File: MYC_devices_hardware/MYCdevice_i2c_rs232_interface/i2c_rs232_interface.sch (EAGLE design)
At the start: 60 parts, among them IC1 MEGA32-P, IC2 MAX232, IC3 7805TV, Q1 20MHz, T1 BC817, T2 BC817, T3 BC817, T4 BC807, T5 BC817-40LT1SMD, T6 BC817-40LT1SMD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

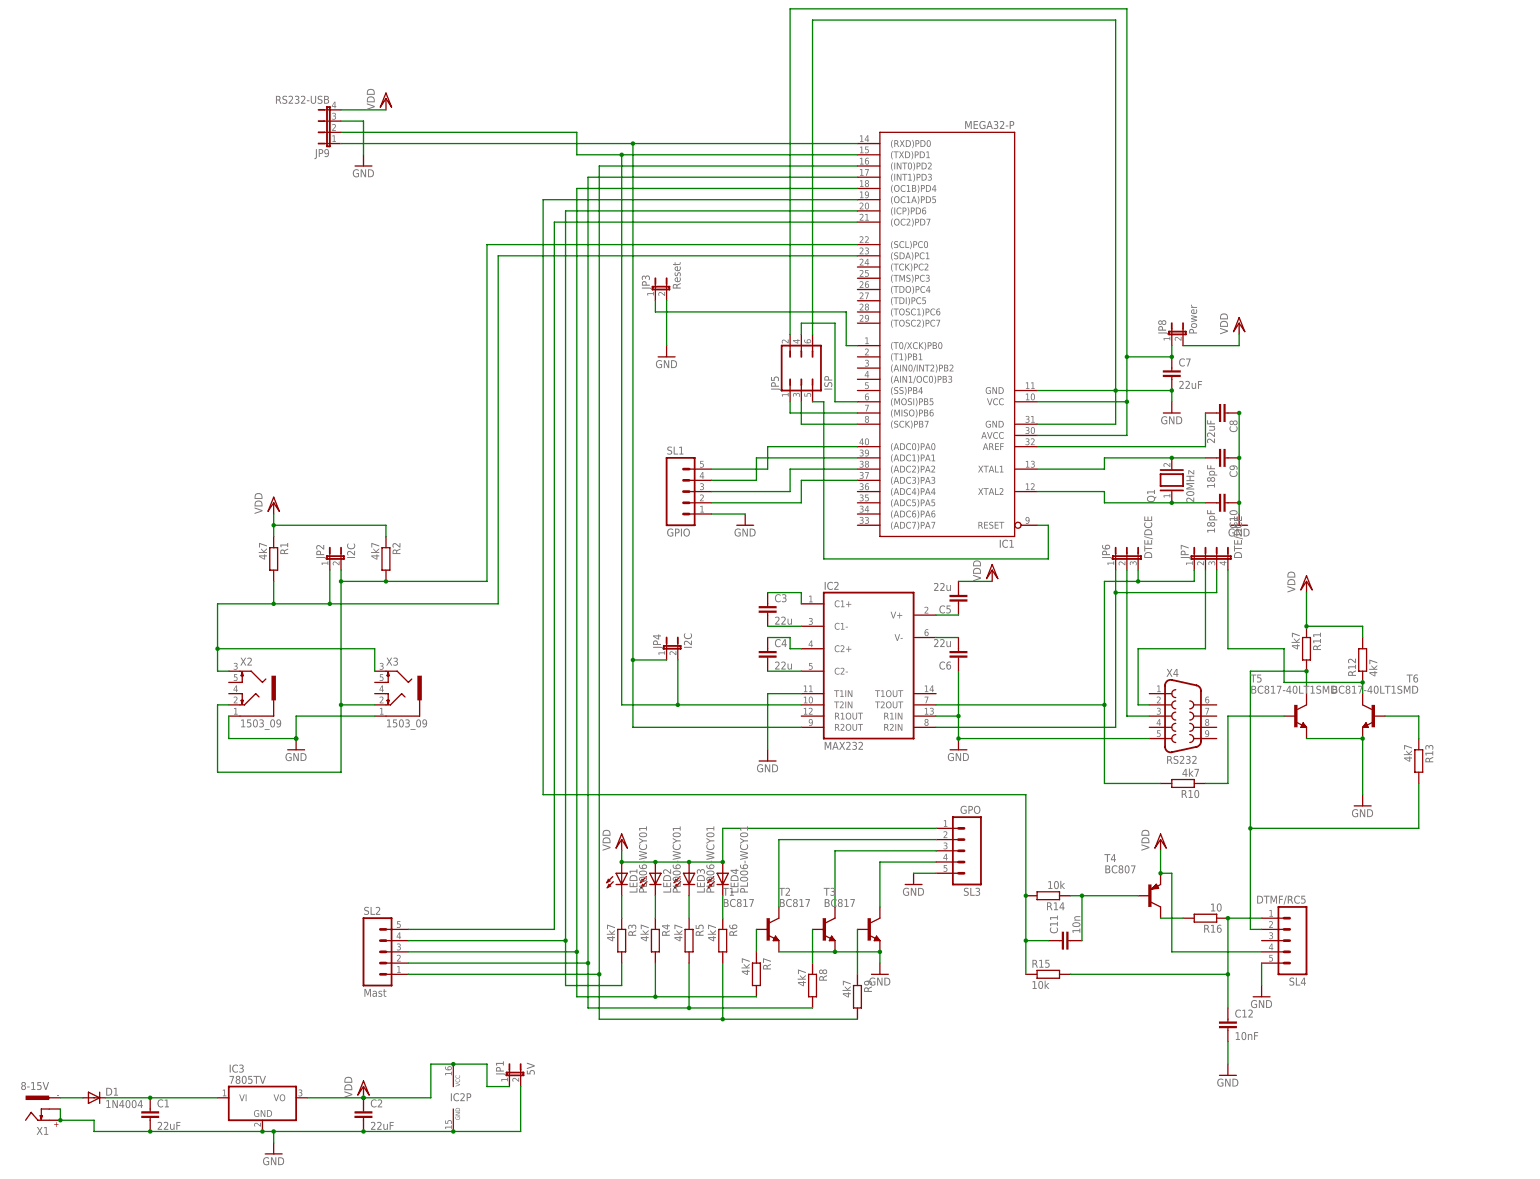
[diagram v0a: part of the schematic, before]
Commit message: HW changed and 254 /255 command croorected
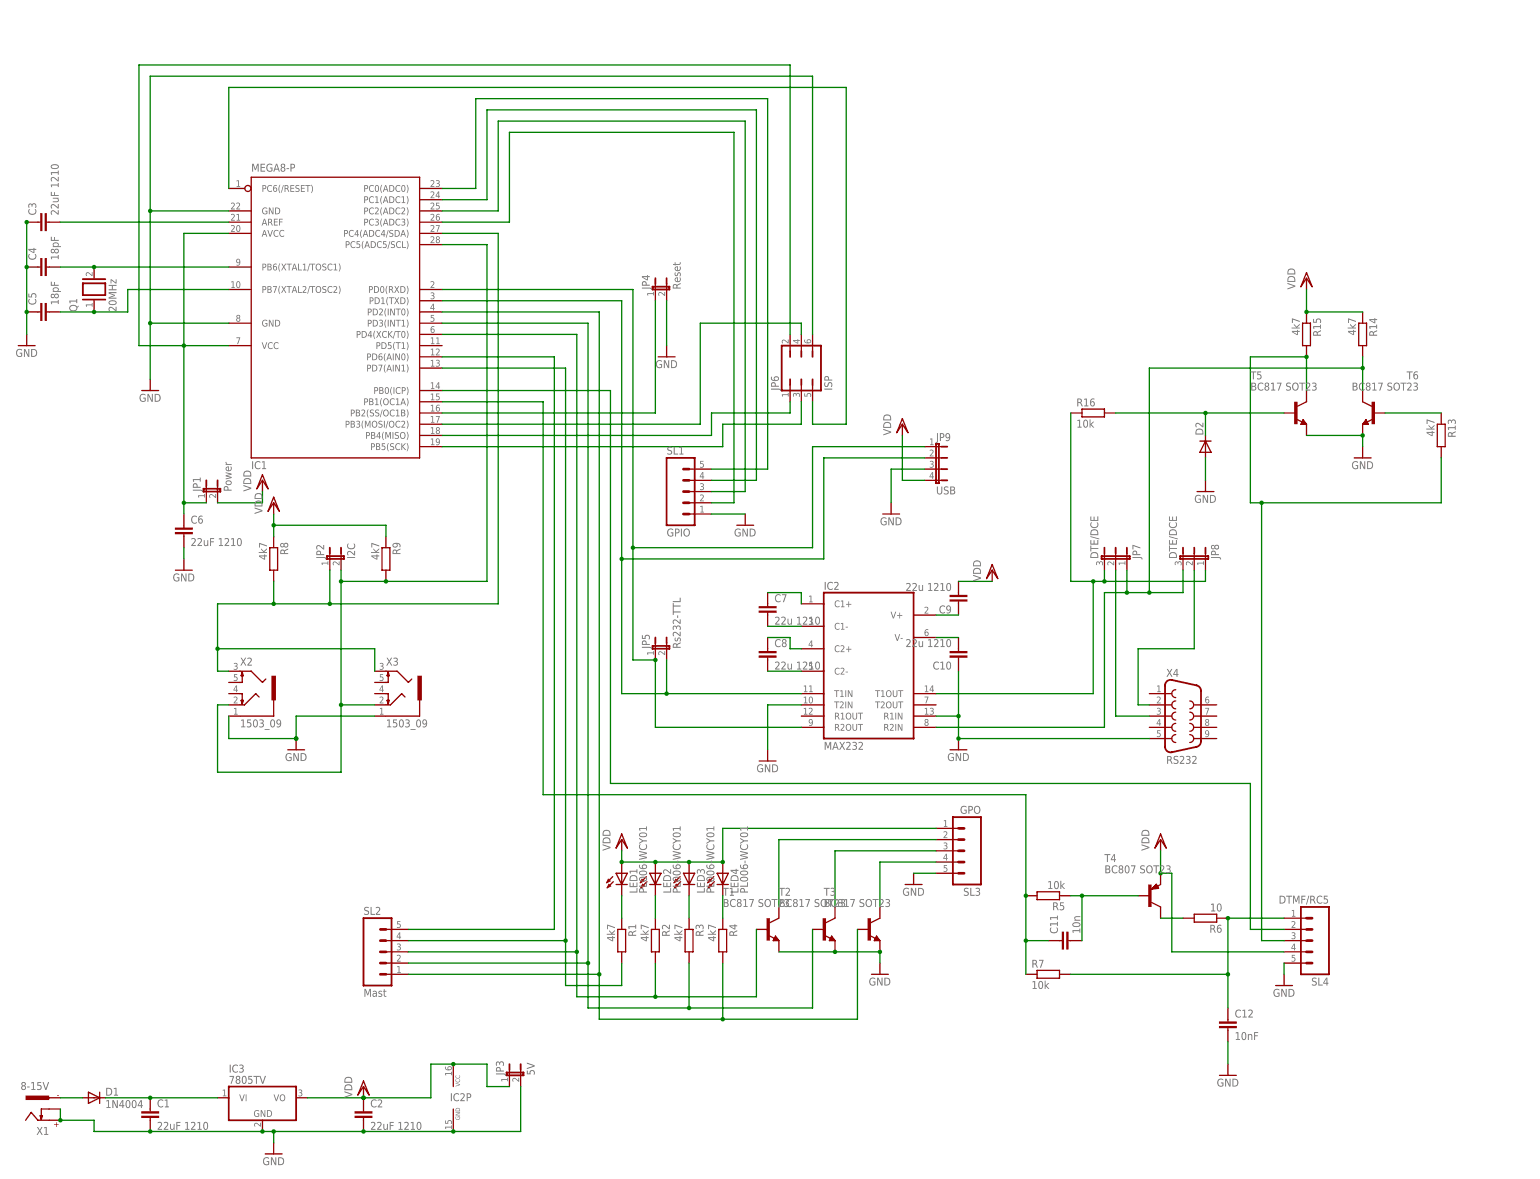
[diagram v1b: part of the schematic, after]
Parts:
- removed R10, R11, R12: 4k7, resistor:R-EU_0207/5V
- added D2: (no value), diode:DIODE-SOD106-R
- C1, C2: value 22uF -> 22uF 1210
- C10, C9: value 18pF -> 22u 1210; device resistor:C-EU025-025X050 -> rcl:C-EUC1206
- C3, C6: value 22u -> 22uF 1210
- C4, C5: value 22u -> 18pF; device rcl:C-EUC1206 -> resistor:C-EU025-025X050
- C7, C8: value 22uF -> 22u 1210
- IC1: value MEGA32-P -> MEGA8-P; device atmel:MEGA32-P -> atmel:MEGA8-P
- JP1: value 5V -> Power
- JP3: value Reset -> 5V
- JP4: value I2C -> Reset
- JP5: value ISP -> Rs232-TTL; device jumper:JP3Q -> jumper:JP1E
- JP6: value DTE/DCE -> ISP; device jumper:JP2E -> jumper:JP3Q
- JP7: device jumper:JP4E -> jumper:JP2E
- JP8: value Power -> DTE/DCE; device jumper:JP1E -> jumper:JP2E
- JP9: value RS232-USB -> USB
- R1, R13, R2, R3, R4: device resistor:R-EU_0207/5V -> resistor:R-EU_R1206
- R14, R15: value 10k -> 4k7; device resistor:R-EU_0207/5V -> resistor:R-EU_R1206
- R16: value 10 -> 10k; device resistor:R-EU_0207/5V -> resistor:R-EU_R1206
- R5, R7: value 4k7 -> 10k
- R6: value 4k7 -> 10
- T1, T2, T3: value BC817 -> BC817 SOT23
- T4: value BC807 -> BC807 SOT23
- T5, T6: value BC817-40LT1SMD -> BC817 SOT23; device transistor-npn:BC817-40LT1SMD -> transistor:BC817-NPN-SOT23-BEC
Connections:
- removed net N$11: IC2G$1.R2IN, JP6.1, JP7.3
- removed net N$21: JP7.4, R12.1, T6.C
- removed net N$24: R7.1, T1.B
- removed net N$27 (its old number): IC1.(RXD)PD0, IC2G$1.R2OUT, JP4.1, JP9.1
- removed net N$36: R11.2, R13.2, SL4.2, T5.C
- removed net N$40: R9.1, T3.B
- removed net N$42 (its old number): C8.2, IC1.AREF
- removed net N$55: C10.2, IC1.XTAL2, Q1.1
- removed net N$58: C7.1, IC1.AVCC, IC1.VCC, JP5.2, JP8.1
- new net N$10: IC2G$1.T1OUT, JP7.3, JP8.1, R16.1
- new net N$37: C5.2, IC1.PB7(XTAL2/TOSC2), Q1.1
- new net N$38: D2.C, R16.2, T5.B
- new net N$44: C6.1, IC1.AVCC, IC1.VCC@1, JP1.1, JP6.2
- new net N$53: R13.2, R15.2, SL4.3, T5.C
- new net N$7: IC1.PB0(ICP), SL4.2
- net C13: now also C7.1; no longer C3.1
- net GND: now also C3.1, C4.1, C5.1, C6.2, D2.A, IC2G$1.T2IN, JP4.2, JP6.6; no longer C6.1, C7.2, C8.1, C9.1, IC2G$1.T1IN, JP1.2, JP5.6
- net N$1: now also IC1.PD7(AIN1), R1.2; no longer IC1.(ICP)PD6, R3.2
- net N$12: now also IC1.PD1(TXD), IC2G$1.T1IN, JP5.2, JP9.2; no longer R8.1, T2.B
- net N$13: now also C8.1; no longer C4.1
- net N$14: now also C7.2; no longer C3.2
- net N$15: now also IC1.PB4(MISO), JP6.1; no longer IC1.(MISO)PB6, JP5.1
- net N$16: now also C9.1; no longer C5.1
- net N$17: now also C10.2; no longer C6.2
- net N$18: now also IC1.PC6(/RESET), JP6.5; no longer IC1.RESET, JP5.5
- net N$19: now also C4.2, IC1.PB6(XTAL1/TOSC1); no longer C9.2, IC1.XTAL1
- net N$2: now also IC1.PD0(RXD), IC2G$1.R2OUT, JP5.1, JP9.1; no longer IC2G$1.T2OUT, JP6.3, JP7.1, R10.2
- net N$20: now also IC1.PB5(SCK), JP6.3; no longer IC1.(SCK)PB7, JP5.3
- net N$22: now also IC1.PC5(ADC5/SCL), R9.2; no longer IC1.(SCL)PC0, R2.2
- net N$23: now also IC1.PD4(XCK/T0), R2.2, T1.B; no longer IC1.(OC1B)PD4, R4.2, R7.2
- net N$25: now also IC1.PC1(ADC1); no longer IC1.(ADC1)PA1
- net N$26: now also IC1.PC2(ADC2); no longer IC1.(ADC2)PA2
- net N$28: now also IC1.PB3(MOSI/OC2), JP6.4; no longer IC1.(MOSI)PB5, JP5.4
- net N$29: now also R5.1; no longer R14.1
- net N$3: now also C8.2; no longer C4.2
- net N$30: now also IC1.PB1(OC1A), R5.2, R7.1; no longer IC1.(OC1A)PD5, R14.2, R15.1
- net N$31: now also R6.2; no longer R16.2
- net N$32: now also R6.1, R7.2; no longer R15.2, R16.1
- net N$34: now also IC1.PC0(ADC0); no longer IC1.(ADC0)PA0
- net N$35: now also C3.2, IC1.AREF; no longer IC1.(TXD)PD1, IC2G$1.T2IN, JP4.2, JP9.2
- net N$39: now also IC1.PC3(ADC3); no longer IC1.(ADC3)PA3
- net N$4: now also JP8.2; no longer JP7.2
- net N$41: now also IC2G$1.R2IN, JP7.1, JP8.3, R14.2, T6.C; no longer R10.1, T5.B
- net N$43: now also R4.1; no longer R6.1
- net N$48: now also R3.1; no longer R5.1
- net N$49: now also R2.1; no longer R4.1
- net N$5: now also IC1.PC4(ADC4/SDA), R8.2; no longer IC1.(SDA)PC1, R1.2
- net N$50: now also R1.1; no longer R3.1
- net N$51: now also IC1.PD3(INT1), R3.2, T2.B; no longer IC1.(INT1)PD3, R5.2, R8.2
- net N$52: now also IC1.PD2(INT0), R4.2, T3.B; no longer IC1.(INT0)PD2, R6.2, R9.2
- net N$6: now also IC1.PB2(SS/OC1B), JP4.1; no longer IC1.(T0/XCK)PB0, JP3.1
- net N$8: now also IC1.PD6(AIN0); no longer IC1.(OC2)PD7
- net N$9: now also JP7.2; no longer JP6.2
- net VDD: now also C9.2, JP1.2, JP3.1, R14.1, R15.1, R8.1, R9.1; no longer C5.2, JP1.1, JP8.2, R1.1, R11.1, R12.2, R2.1
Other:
- moved on the sheet: C10, C3, C4, C5, C6, C7, C8, C9, JP1, JP3, JP4, JP9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
